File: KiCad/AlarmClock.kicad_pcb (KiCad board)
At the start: 2 copper layers, 75 parts, among them SW1 RotaryEncoder_Switch, SW2 SW_SPST, SW3 SW_Push, U1 D168K, U10 TPIC6595, U11 TPIC6595, U12 TPIC6595, U13 TPIC6595, U14 TPIC6595, U15 TPIC6595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

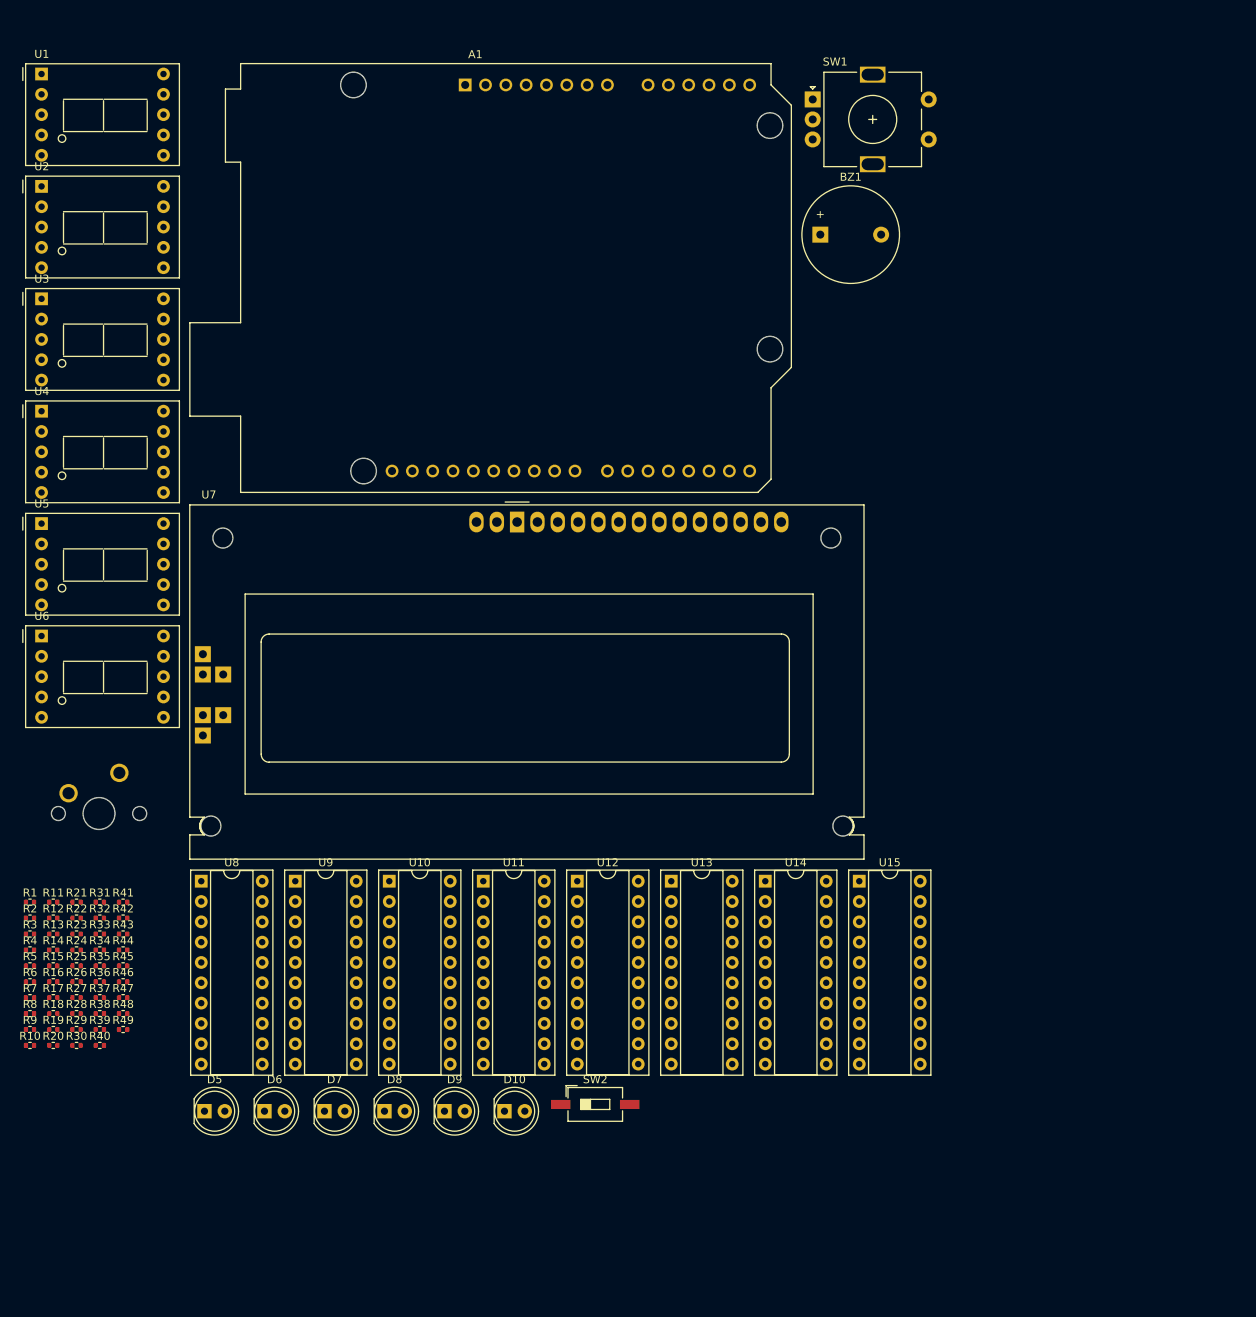
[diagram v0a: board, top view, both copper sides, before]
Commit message: Update schematic to adhere to ERC
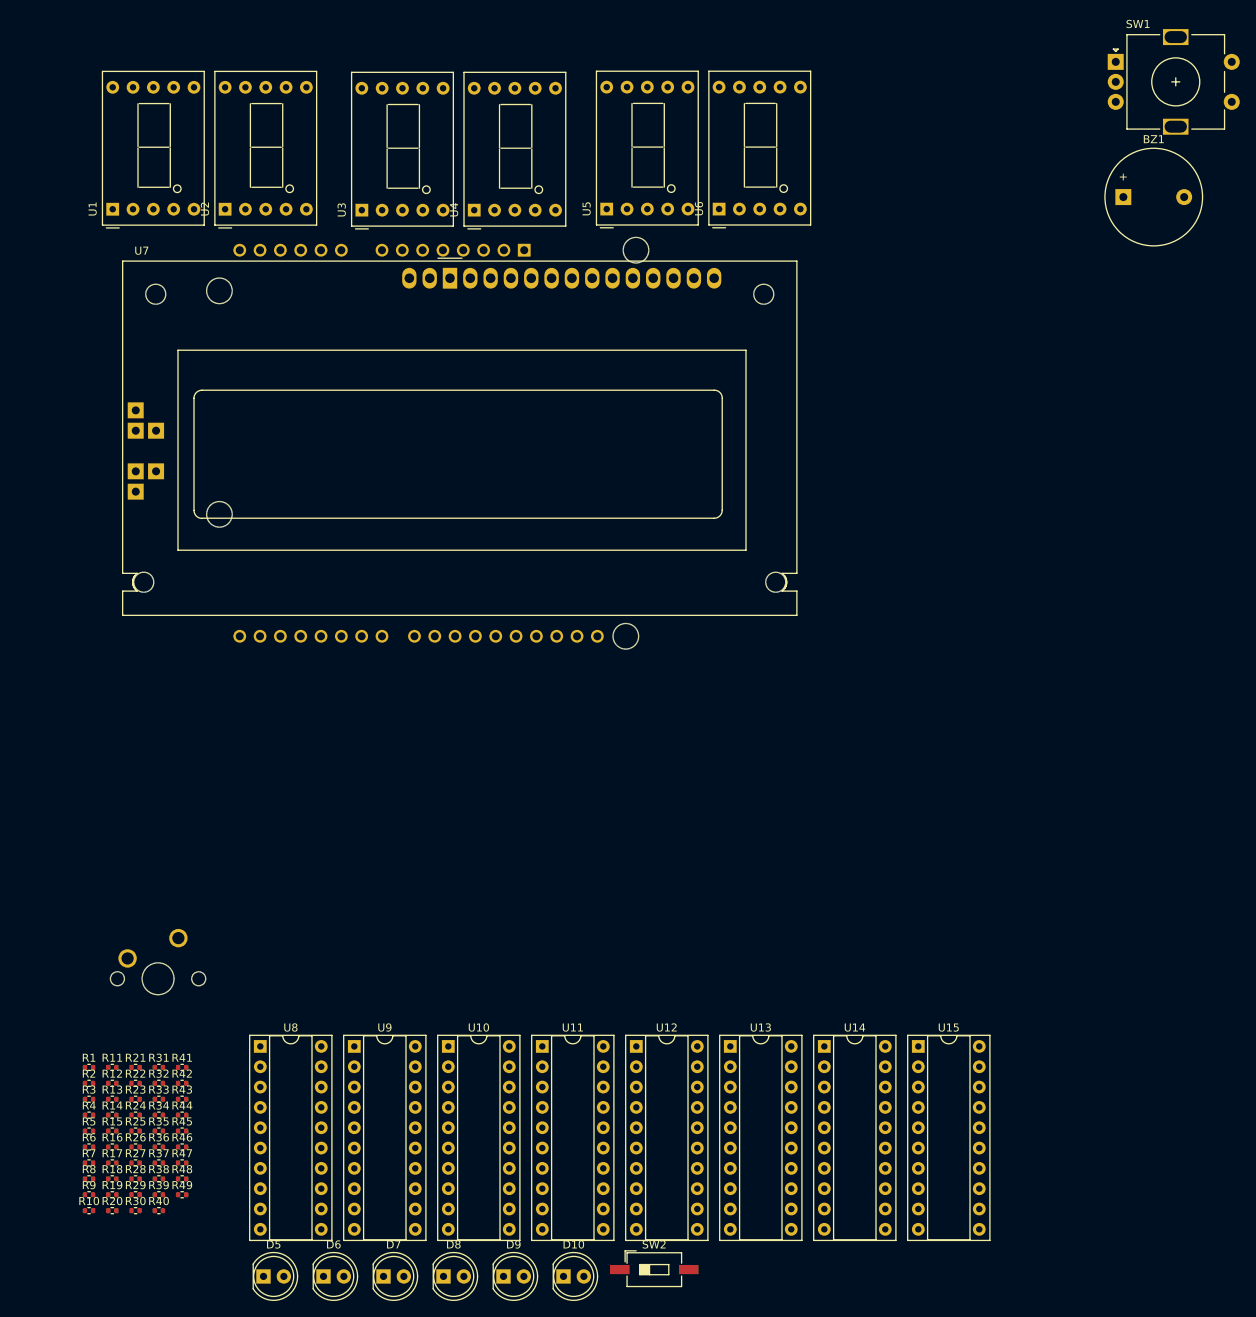
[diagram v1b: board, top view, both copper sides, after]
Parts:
- A1: moved to B.Cu
- moved U6 100.1 mm to (166.1, 51.4), turned to 90 degrees
- moved U5 80.8 mm to (152.0, 51.4), turned to 90 degrees
- moved U4 59.6 mm to (135.4, 51.5), turned to 90 degrees
- moved U3 41.5 mm to (121.4, 51.5), turned to 90 degrees
- moved BZ1 38.2 mm to (216.6, 49.9)
- moved SW1 38.2 mm to (215.6, 33.0)
- moved U7 31.6 mm to (132.4, 60.0)
- moved U2 23.1 mm to (104.3, 51.4), turned to 90 degrees
- moved SW3 21.9 mm to (95.9, 147.6)
- moved R1 21.9 mm to (87.3, 158.7)
- moved R10 21.9 mm to (87.3, 176.6)
- moved R11 21.9 mm to (90.2, 158.7)
- moved R12 21.9 mm to (90.2, 160.7)
- moved R13 21.9 mm to (90.2, 162.7)
- moved R14 21.9 mm to (90.2, 164.7)
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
